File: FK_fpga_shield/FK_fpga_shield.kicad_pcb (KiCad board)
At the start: 4 copper layers, 182 x 125 mm, 158 parts, among them J0 USB_B_Mini, J1 molex-51382-0400-microclasp, J10 molex-51382-0400-microclasp, J11 molex-51382-0400-microclasp, J12 molex-51382-0400-microclasp, J13 molex-51382-0400-microclasp, J14 molex-51382-0400-microclasp, J15 molex-51382-0400-microclasp, J16 molex-51382-0400-microclasp, J17 molex-51382-0400-microclasp, J18 molex-51382-0400-microclasp, J19 molex-51382-0400-microclasp, J2 molex-51382-0400-microclasp, J20 molex-51382-0400-microclasp, J21 molex-51382-0400-microclasp, J22 molex-51382-0400-microclasp, J23 molex-51382-0400-microclasp, J24 molex-51382-0400-microclasp, J25 molex-51382-0400-microclasp, J26 molex-51382-0400-microclasp, J27 molex-51382-0400-microclasp, J28 molex-51382-0400-microclasp, J29 molex-51382-0400-microclasp, J3 molex-51382-0400-microclasp, J30 molex-51382-0400-microclasp, J31 molex-51382-0400-microclasp, J32 molex-51382-0400-microclasp, J33 molex-51382-0400-microclasp, J34 molex-51382-0400-microclasp, J35 molex-51382-0400-microclasp, J36 Barrel_Jack_MountingPin, J4 molex-51382-0400-microclasp, J5 molex-51382-0400-microclasp, J6 molex-51382-0400-microclasp, J7 molex-51382-0400-microclasp, J8 molex-51382-0400-microclasp, J9 molex-51382-0400-microclasp, U1 FT232RL, U2 nvt2010pw, U3 nvt2010pw, U4 nvt2010pw, U5 nvt2010pw, U6 nvt2010pw, U7 nvt2010pw, U8 nvt2010pw, Y1 DNP_(12MHz)

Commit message: choosen choke
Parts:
- added H3: MountingHole, MountingHole:MountingHole_3mm, F.Cu at (78.8, 53.6)
- added H4: MountingHole, MountingHole:MountingHole_3mm, F.Cu at (253.8, 53.1)
- added H5: MountingHole, MountingHole:MountingHole_3mm, F.Cu at (78.8, 148.9)
- added H6: MountingHole, MountingHole:MountingHole_3mm, F.Cu at (253.8, 148.9)
- added L1: WE_744823422, Inductor_THT:L_CommonMode_Wuerth_WE-CMB-M, F.Cu at (84.4, 81.8)
- moved C26 8.93 mm to (104.4, 99.4)
- moved C28 8.93 mm to (111.2, 99.4)
- moved C29 8.93 mm to (114.4, 99.4)
- moved C21 8.93 mm to (100.6, 93.2)
- moved C22 8.93 mm to (109.1, 93.2)
- moved C23 8.93 mm to (117.6, 93.2)
- moved C24 8.93 mm to (126.1, 93.2)
- moved C25 8.93 mm to (101.0, 99.4)
- moved C27 8.93 mm to (107.8, 99.4)
- moved C30 8.93 mm to (117.6, 99.4)
- moved C31 8.93 mm to (120.8, 99.4)
- moved J36 8.60 mm to (87.6, 104.2)
- moved R48 1.40 mm to (84.0, 53.0)
- moved R43 1.40 mm to (87.8, 53.0)
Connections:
- J36 pad 1: /5V -> Net-(J36-Pad1)
- J36 pad 2: GND -> Net-(J36-Pad2)
- J36 pad MP: GND -> Net-(J36-Pad2)
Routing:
- net /5V: track 330.1 -> 326.3 mm
- net Net-(J1-Pad2): track 29.2 -> 30.0 mm
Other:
- board text added: "PIN A8"
- board text added: "PIN T9"
- board text added: "RX"
- board text added: "TX"

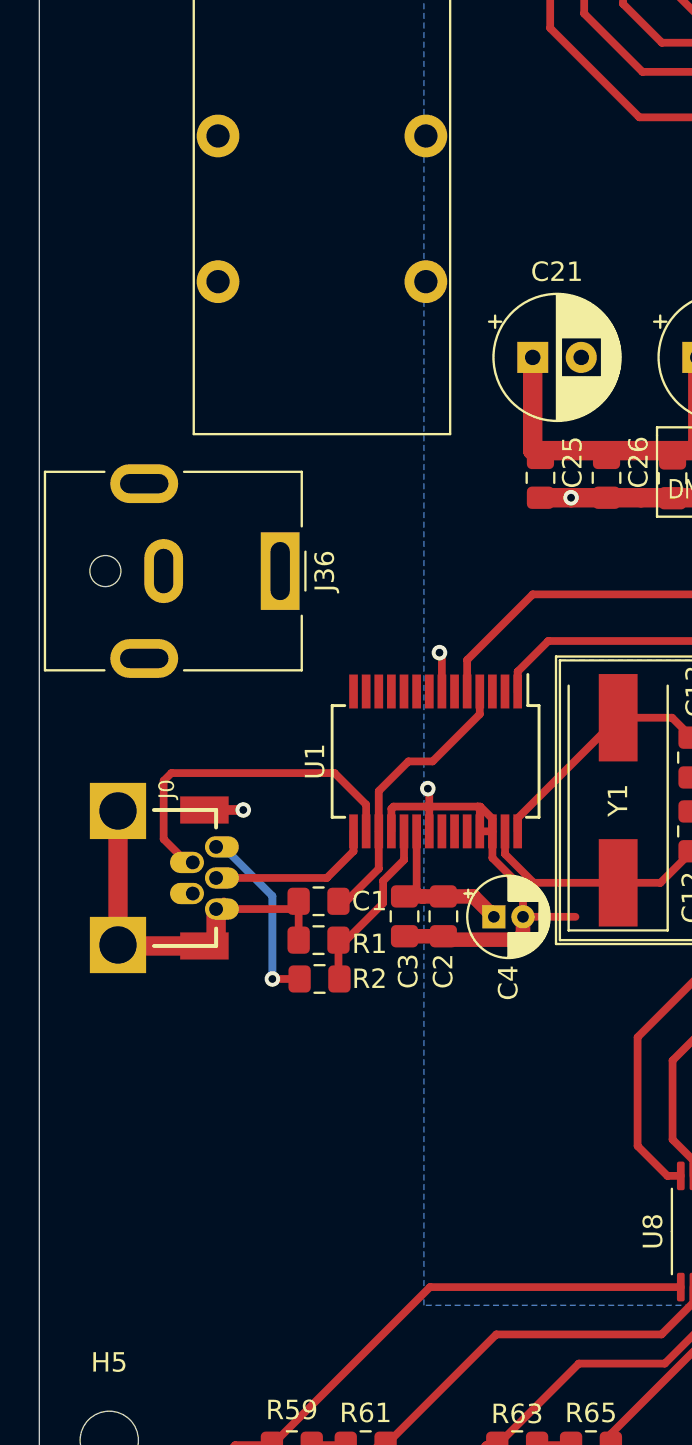
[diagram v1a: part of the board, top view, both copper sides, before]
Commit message: 2x4 breakout header for uart convertor, choke laid out
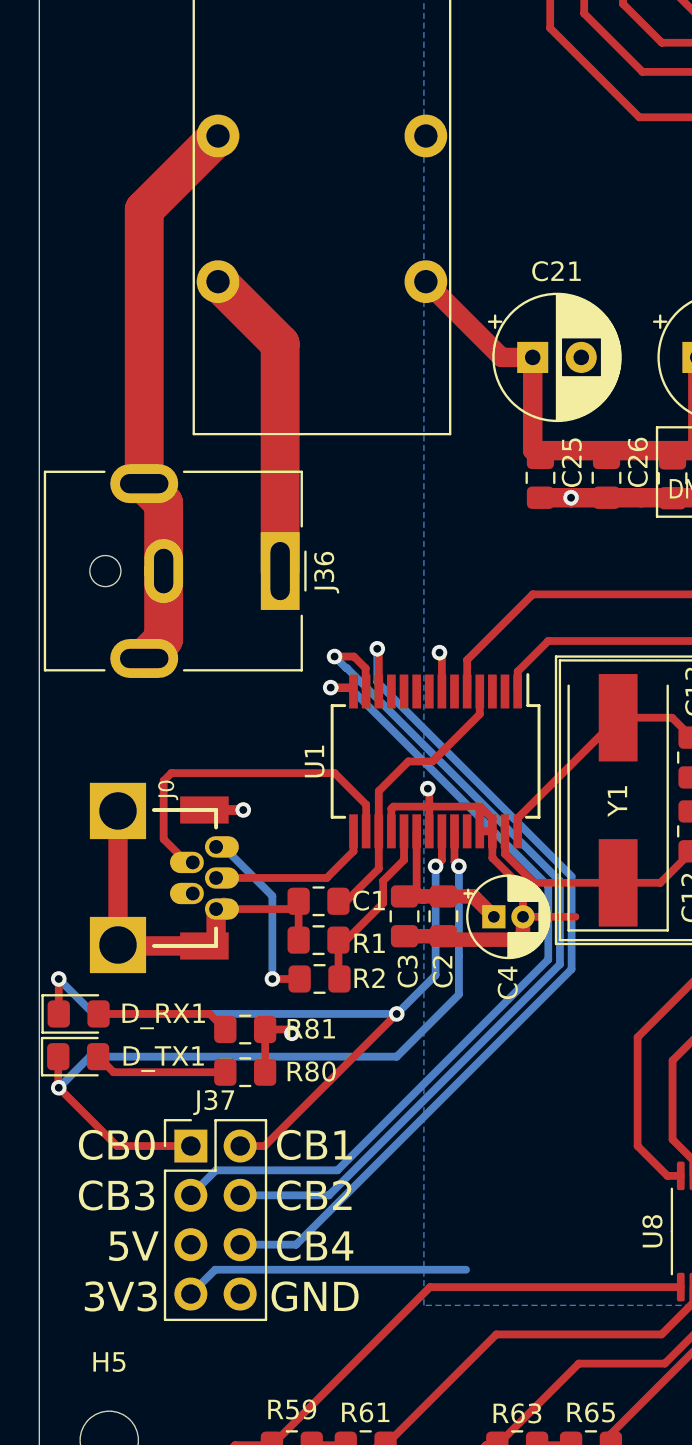
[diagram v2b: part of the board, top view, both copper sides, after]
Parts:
- added D_RX1: LED RX, LED_SMD:LED_0805_2012Metric_Pad1.15x1.40mm_HandSolder, F.Cu at (77.2, 127.0)
- added D_TX1: LED_TX, LED_SMD:LED_0805_2012Metric_Pad1.15x1.40mm_HandSolder, F.Cu at (77.2, 129.2)
- added J37: Conn_02x04_Top_Bottom, Connector_PinHeader_2.54mm:PinHeader_2x04_P2.54mm_Vertical, F.Cu at (83.0, 133.8)
- added R80: 270, Resistor_SMD:R_0805_2012Metric_Pad1.15x1.40mm_HandSolder, F.Cu at (85.8, 130.0)
- added R81: 270, Resistor_SMD:R_0805_2012Metric_Pad1.15x1.40mm_HandSolder, F.Cu at (85.8, 127.8)
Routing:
- net Net-(J37-Pad6): track 0.00 -> 45.8 mm, vias 0 -> 1
- net Net-(J37-Pad4): track 0.00 -> 45.1 mm, vias 0 -> 1
- net Net-(J37-Pad3): track 0.00 -> 43.9 mm, vias 0 -> 1
- net Net-(D_RX1-Pad1): track 0.00 -> 41.2 mm, vias 0 -> 3
- net Net-(D_TX1-Pad1): track 0.00 -> 40.7 mm, vias 0 -> 2
- net Net-(J36-Pad2): track 0.00 -> 29.3 mm
- net Net-(J36-Pad1): track 0.00 -> 16.2 mm
- net /3V3: track 33.3 -> 48.0 mm
- net /5V: track 326.3 -> 337.1 mm, vias 7 -> 8
- net Net-(D_TX1-Pad2): track 0.00 -> 6.88 mm
- net Net-(D_RX1-Pad2): track 0.00 -> 6.86 mm
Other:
- board text added: "CB0"
- board text added: "CB1"
- board text added: "CB2"
- board text added: "CB3"
- board text added: "CB4"

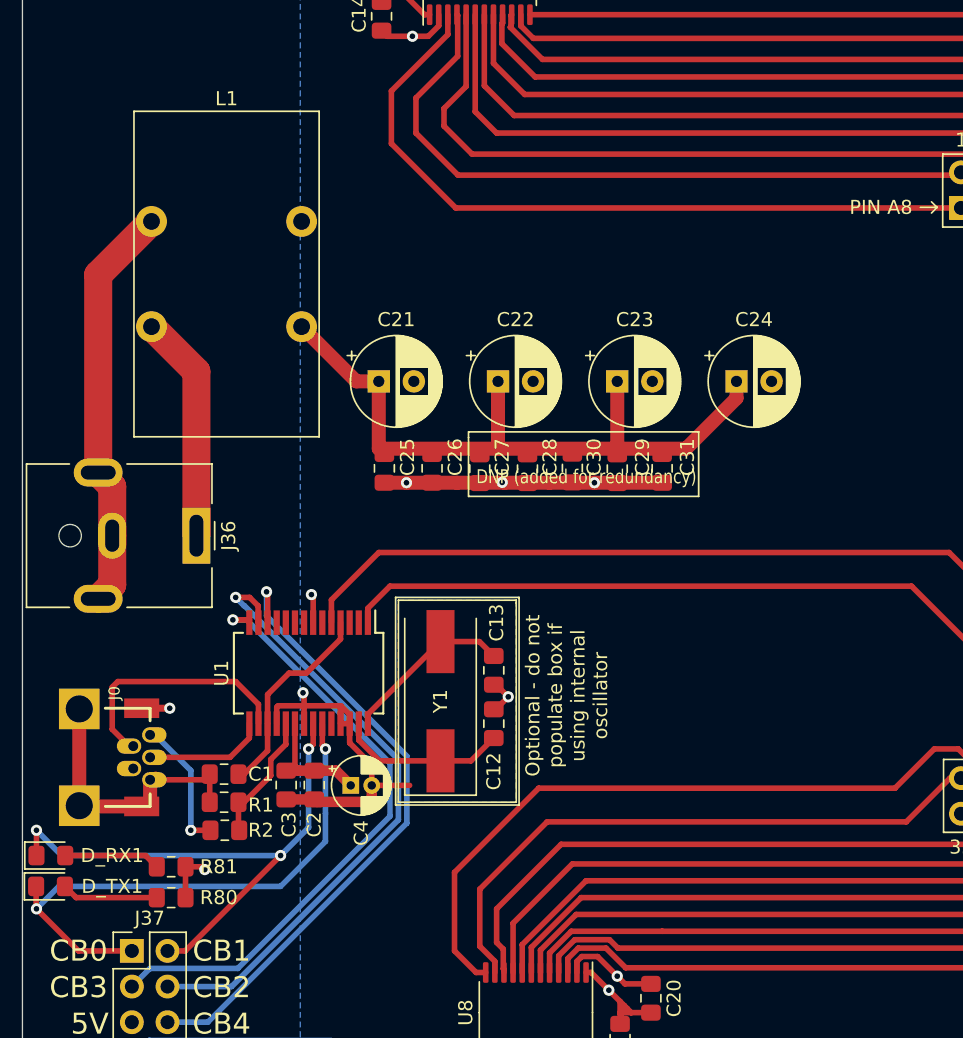
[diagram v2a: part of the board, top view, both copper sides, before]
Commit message: replace common mode choke with filter
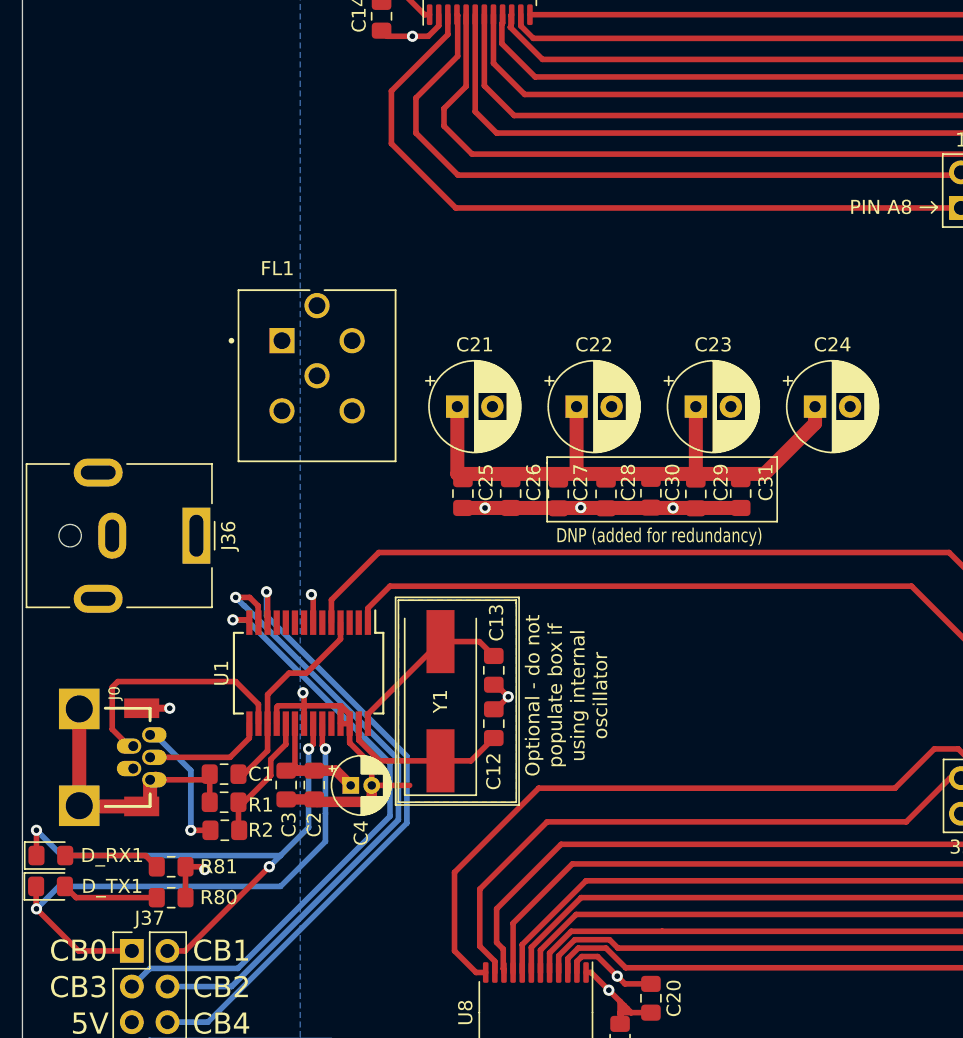
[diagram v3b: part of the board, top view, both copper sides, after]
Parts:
- removed L1: WE_744823422, Inductor_THT:L_CommonMode_Wuerth_WE-CMB-M
- added FL1: BNX016-01, FK_fpga_shield_custom_footprints:FIL_BNX016-01, F.Cu at (96.2, 92.8)
- moved C21 5.88 mm to (106.2, 95.0)
- moved C22 5.88 mm to (114.7, 95.0)
- moved C23 5.88 mm to (123.2, 95.0)
- moved C27 5.88 mm to (113.4, 101.2)
- moved C30 5.88 mm to (123.2, 101.2)
- moved C31 5.88 mm to (126.4, 101.2)
- moved C24 5.88 mm to (131.7, 95.0)
- moved C25 5.88 mm to (106.6, 101.2)
- moved C26 5.88 mm to (110.0, 101.2)
- moved C28 5.88 mm to (116.8, 101.2)
- moved C29 5.88 mm to (120.0, 101.2)
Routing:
- net Net-(FL1-Pad3): track 29.3 -> 0.00 mm
- net Net-(FL1-Pad1): track 16.2 -> 0.00 mm
- net /5V: track 337.1 -> 329.9 mm

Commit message: various minor
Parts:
- J1, J10, J11, J12, J13, J14, J15, J16, J17, J18, J19, J2, J20, J21, J22, J23, J24, J25, J26, J27, J28, J29, J3, J30, J31, J32, J33, J34, J35, J4, J5, J6, J7, J8, J9: footprint FK_fpga_shield_custom_footprints:Molex_MicroClasp_55935-0410_1x04_P2.00mm_Horizontal_3DMODEL -> Connector_Molex:Molex_MicroClasp_55935-0410_1x04_P2.00mm_Horizontal
- moved J36 9.60 mm to (87.6, 94.6)
- moved FL1 4.04 mm to (96.8, 96.8)
- moved J37 3.82 mm to (86.8, 134.2)
- moved R78 3.60 mm to (181.4, 140.6)
- moved R79 3.00 mm to (124.0, 141.0)
- moved R53 2.80 mm to (96.2, 61.4)
- moved C18 2.23 mm to (209.6, 123.2)
- moved C14 2.11 mm to (101.4, 69.2), turned to 315 degrees
- moved R56 2.00 mm to (223.4, 90.0)
- moved R55 1.96 mm to (213.9, 61.6), turned to 315 degrees
- moved R54 1.80 mm to (158.0, 61.2)
- moved R57 1.80 mm to (217.8, 119.2)
- moved C19 1.02 mm to (174.6, 134.0)
- moved C17 0.82 mm to (215.8, 94.4)
- moved C16 0.74 mm to (209.4, 65.6), turned to 225 degrees
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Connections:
- FL1 pad 4: Net-(FL1-Pad4) -> GND
- FL1 pad 5: Net-(FL1-Pad5) -> GND
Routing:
- net /3V3: track 48.0 -> 72.2 mm
- net Net-(FL1-Pad3): track 0.00 -> 23.9 mm
- net GND: track 126.0 -> 139.4 mm
- net /5V: track 329.9 -> 339.7 mm
- net Net-(FL1-Pad1): track 0.00 -> 6.82 mm
- net Net-(D_TX1-Pad1): track 40.7 -> 44.7 mm
- net Net-(J37-Pad3): track 43.9 -> 40.3 mm
- net Net-(C10-Pad1): track 5.43 -> 9.03 mm
- net Net-(J37-Pad4): track 45.1 -> 41.5 mm
- net Net-(C11-Pad1): track 5.30 -> 8.30 mm
- net Net-(J37-Pad6): track 45.8 -> 42.9 mm
- net Net-(C5-Pad1): track 5.18 -> 7.98 mm
- net Net-(C7-Pad1): track 6.51 -> 8.65 mm
- net Net-(C8-Pad1): track 4.95 -> 6.95 mm
- net Net-(D_RX1-Pad1): track 41.2 -> 39.3 mm
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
